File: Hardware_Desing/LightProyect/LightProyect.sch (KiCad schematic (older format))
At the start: 10 parts

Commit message: schematics changes
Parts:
- D1: renamed from D?; footprint (none) -> LightProyect:Neopixel
- J1, J3: renamed from J?; footprint (none) -> TerminalBlock:TerminalBlock_bornier-3_P5.08mm
- J2: renamed from J?; footprint (none) -> TerminalBlock:TerminalBlock_Altech_AK300-3_P5.00mm
- M1: renamed from M?; footprint (none) -> LightProyect:YP8AMS1117_5v_3_3_V
- M2: renamed from M?; footprint (none) -> LightProyect:DC_DC_5V_3V_module
- M3: renamed from M?; footprint (none) -> LightProyect:Audio_Senso_module
- M4: renamed from M?; footprint (none) -> LightProyect:GY-521
- SW1: renamed from SW?; footprint (none) -> Button_Switch_SMD:SW_SPST_TL3305C
- gave numbers to parts that had none: 1
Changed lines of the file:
@@
 $EndDescr
 $Comp
-L power:PWR_FLAG #FLG?
+L power:PWR_FLAG #FLG01
 U 1 1 5EE98E5D
 P 2250 1450
-F 0 "#FLG?" H 2250 1525 50  0001 C CNN
+F 0 "#FLG01" H 2250 1525 50  0001 C CNN
 F 1 "PWR_FLAG" H 2250 1623 50  0000 C CNN
 F 2 "" H 2250 1450 50  0001 C CNN
@@
 $EndComp
 $Comp
-L power:PWR_FLAG #FLG?
+L power:PWR_FLAG #FLG02
 U 1 1 5EE98FDA
 P 3400 3600
-F 0 "#FLG?" H 3400 3675 50  0001 C CNN
+F 0 "#FLG02" H 3400 3675 50  0001 C CNN
 F 1 "PWR_FLAG" H 3350 3750 50  0000 C CNN
 F 2 "" H 3400 3600 50  0001 C CNN
@@
 $EndComp
 $Comp
-L power:VCC #PWR?
+L power:VCC #PWR01
 U 1 1 5EE9959C
 P 1950 1500
-F 0 "#PWR?" H 1950 1350 50  0001 C CNN
+F 0 "#PWR01" H 1950 1350 50  0001 C CNN
 F 1 "VCC" H 1950 1700 50  0000 C CNN
 F 2 "" H 1950 1500 50  0001 C CNN
@@
 $EndComp
 $Comp
-L power:GND #PWR?
+L power:GND #PWR02
 U 1 1 5EE99A46
 P 2700 3600
-F 0 "#PWR?" H 2700 3350 50  0001 C CNN
+F 0 "#PWR02" H 2700 3350 50  0001 C CNN
 F 1 "GND" H 2705 3427 50  0000 C CNN
 F 2 "" H 2700 3600 50  0001 C CNN
@@
 $EndComp
 $Comp
-L RF_Module:ESP-12E U?
+L RF_Module:ESP-12E U1
 U 1 1 5EE9A169
 P 5500 3150
-F 0 "U?" H 5500 4131 50  0000 C CNN
+F 0 "U1" H 5500 4131 50  0000 C CNN
 F 1 "ESP-12E" H 5500 4040 50  0000 C CNN
 F 2 "RF_Module:ESP-12E" H 5500 3150 50  0001 C CNN
@@
 Connection ~ 3400 3600
 $Comp
-L DC_DC_3_5_V_Module:DC_DC_3_5_module M?
+L DC_DC_3_5_V_Module:DC_DC_3_5_module M2
 U 1 1 5EE9F569
 P 3800 1450
-F 0 "M?" H 3912 1815 50  0000 C CNN
+F 0 "M2" H 3912 1815 50  0000 C CNN
 F 1 "DC_DC_3_5_module" H 3912 1724 50  0000 C CNN
-F 2 "" H 3900 1800 50  0001 C CNN
+F 2 "LightProyect:DC_DC_5V_3V_module" H 3900 1800 50  0001 C CNN
 F 3 "" H 3900 1800 50  0001 C CNN
 	1    3800 1450
@@
 $EndComp
 $Comp
-L VoltageRegulator_X_3.3:Regulator_x_3_3 M?
+L VoltageRegulator_X_3.3:Regulator_x_3_3 M1
 U 1 1 5EEA2C27
 P 3700 2350
-F 0 "M?" H 3837 2765 50  0000 C CNN
+F 0 "M1" H 3837 2765 50  0000 C CNN
 F 1 "Regulator_x_3_3" H 3837 2674 50  0000 C CNN
-F 2 "" H 3650 2700 50  0001 C CNN
+F 2 "LightProyect:YP8AMS1117_5v_3_3_V" H 3650 2700 50  0001 C CNN
 F 3 "" H 3650 2700 50  0001 C CNN
 	1    3700 2350
@@
 Connection ~ 4350 3600
 $Comp
-L MPU6050_compressed:MPU6050_lite M?
+L MPU6050_compressed:MPU6050_lite M4
 U 1 1 5EEA9A03
 P 6900 3150
-F 0 "M?" H 7178 3071 50  0000 L CNN
+F 0 "M4" H 7178 3071 50  0000 L CNN
 F 1 "MPU6050_lite" H 7178 2980 50  0000 L CNN
-F 2 "" H 6900 3400 50  0001 C CNN
+F 2 "LightProyect:GY-521" H 6900 3400 50  0001 C CNN
 F 3 "" H 6900 3400 50  0001 C CNN
 	1    6900 3150
@@
 	6300 2750 6100 2750
 $Comp
-L power:GND #PWR?
+L power:GND #PWR06
 U 1 1 5EEB087B
 P 6600 3250
-F 0 "#PWR?" H 6600 3000 50  0001 C CNN
+F 0 "#PWR06" H 6600 3000 50  0001 C CNN
 F 1 "GND" V 6605 3122 50  0000 R CNN
 F 2 "" H 6600 3250 50  0001 C CNN
@@
 $EndComp
 $Comp
-L Connector:AudioJack2_SwitchT J?
+L Connector:AudioJack2_SwitchT J2
 U 1 1 5EEB712D
 P 2000 2250
-F 0 "J?" H 2032 2575 50  0000 C CNN
+F 0 "J2" H 2032 2575 50  0000 C CNN
 F 1 "AudioJack2_SwitchT" H 2032 2484 50  0000 C CNN
-F 2 "" H 2000 2250 50  0001 C CNN
+F 2 "TerminalBlock:TerminalBlock_Altech_AK300-3_P5.00mm" H 2000 2250 50  0001 C CNN
 F 3 "~" H 2000 2250 50  0001 C CNN
 	1    2000 2250
@@
 	7150 2550 7200 2550
 $Comp
-L power:GND #PWR?
+L power:GND #PWR07
 U 1 1 5EEC104A
 P 7200 2550
-F 0 "#PWR?" H 7200 2300 50  0001 C CNN
+F 0 "#PWR07" H 7200 2300 50  0001 C CNN
 F 1 "GND" V 7205 2422 50  0000 R CNN
 F 2 "" H 7200 2550 50  0001 C CNN
@@
 $EndComp
 $Comp
-L Switch:SW_Push SW?
+L Switch:SW_Push SW1
 U 1 1 5EEBFDC3
 P 6950 2550
-F 0 "SW?" H 6950 2835 50  0000 C CNN
+F 0 "SW1" H 6950 2835 50  0000 C CNN
 F 1 "SW_Push" H 6950 2744 50  0000 C CNN
-F 2 "" H 6950 2750 50  0001 C CNN
+F 2 "Button_Switch_SMD:SW_SPST_TL3305C" H 6950 2750 50  0001 C CNN
 F 3 "~" H 6950 2750 50  0001 C CNN
 	1    6950 2550
@@
 $EndComp
 $Comp
-L Connector:Screw_Terminal_01x03 J?
+L Connector:Screw_Terminal_01x03 J3
 U 1 1 5EEC38D8
 P 7400 2800
-F 0 "J?" H 7480 2842 50  0000 L CNN
+F 0 "J3" H 7480 2842 50  0000 L CNN
 F 1 "Screw_Terminal_01x03" H 7480 2751 50  0000 L CNN
-F 2 "" H 7400 2800 50  0001 C CNN
+F 2 "TerminalBlock:TerminalBlock_bornier-3_P5.08mm" H 7400 2800 50  0001 C CNN
 F 3 "~" H 7400 2800 50  0001 C CNN
 	1    7400 2800
@@
 	6750 2900 7200 2900
 $Comp
-L Connector:Screw_Terminal_01x02 J?
+L Connector:Screw_Terminal_01x02 J1
 U 1 1 5EECC20A
 P 1250 2450
-F 0 "J?" H 1168 2125 50  0000 C CNN
+F 0 "J1" H 1168 2125 50  0000 C CNN
 F 1 "Screw_Terminal_01x02" H 1168 2216 50  0000 C CNN
-F 2 "" H 1250 2450 50  0001 C CNN
+F 2 "TerminalBlock:TerminalBlock_bornier-3_P5.08mm" H 1250 2450 50  0001 C CNN
 F 3 "~" H 1250 2450 50  0001 C CNN
 	1    1250 2450
@@
 	1450 3600 2700 3600
 $Comp
-L AudioModule:AudioModule M?
+L AudioModule:AudioModule M3
 U 1 1 5EED2E37
 P 5150 1400
-F 0 "M?" H 5428 1221 50  0000 L CNN
+F 0 "M3" H 5428 1221 50  0000 L CNN
 F 1 "AudioModule" H 5428 1130 50  0000 L CNN
-F 2 "" H 5150 1400 50  0001 C CNN
+F 2 "LightProyect:Audio_Senso_module" H 5150 1400 50  0001 C CNN
 F 3 "" H 5150 1400 50  0001 C CNN
 	1    5150 1400
@@
 	4350 1550 4700 1550
 $Comp
-L power:GND #PWR?
+L power:GND #PWR03
 U 1 1 5EED4411
 P 4850 1750
-F 0 "#PWR?" H 4850 1500 50  0001 C CNN
+F 0 "#PWR03" H 4850 1500 50  0001 C CNN
 F 1 "GND" V 4855 1622 50  0000 R CNN
 F 2 "" H 4850 1750 50  0001 C CNN
@@
 	4750 3350 4900 3350
 $Comp
-L LED:NeoPixel_THT D?
+L LED:NeoPixel_THT D1
 U 1 1 5EED76D3
 P 6150 1400
-F 0 "D?" H 6494 1446 50  0000 L CNN
+F 0 "D1" H 6494 1446 50  0000 L CNN
 F 1 "NeoPixel_THT" H 6494 1355 50  0000 L CNN
-F 2 "" H 6200 1100 50  0001 L TNN
+F 2 "LightProyect:Neopixel" H 6200 1100 50  0001 L TNN
 F 3 "https://www.adafruit.com/product/1938" H 6250 1025 50  0001 L TNN
 	1    6150 1400
@@
 	4700 1550 4850 1550
 $Comp
-L power:GND #PWR?
+L power:GND #PWR04
 U 1 1 5EED96E6
 P 4850 1750
-F 0 "#PWR?" H 4850 1500 50  0001 C CNN
+F 0 "#PWR04" H 4850 1500 50  0001 C CNN
 F 1 "GND" V 4855 1622 50  0000 R CNN
 F 2 "" H 4850 1750 50  0001 C CNN
@@
 Connection ~ 4850 1750
 $Comp
-L power:GND #PWR?
+L power:GND #PWR05
 U 1 1 5EED9B42
 P 6150 1700
-F 0 "#PWR?" H 6150 1450 50  0001 C CNN
+F 0 "#PWR05" H 6150 1450 50  0001 C CNN
 F 1 "GND" H 6155 1527 50  0000 C CNN
 F 2 "" H 6150 1700 50  0001 C CNN

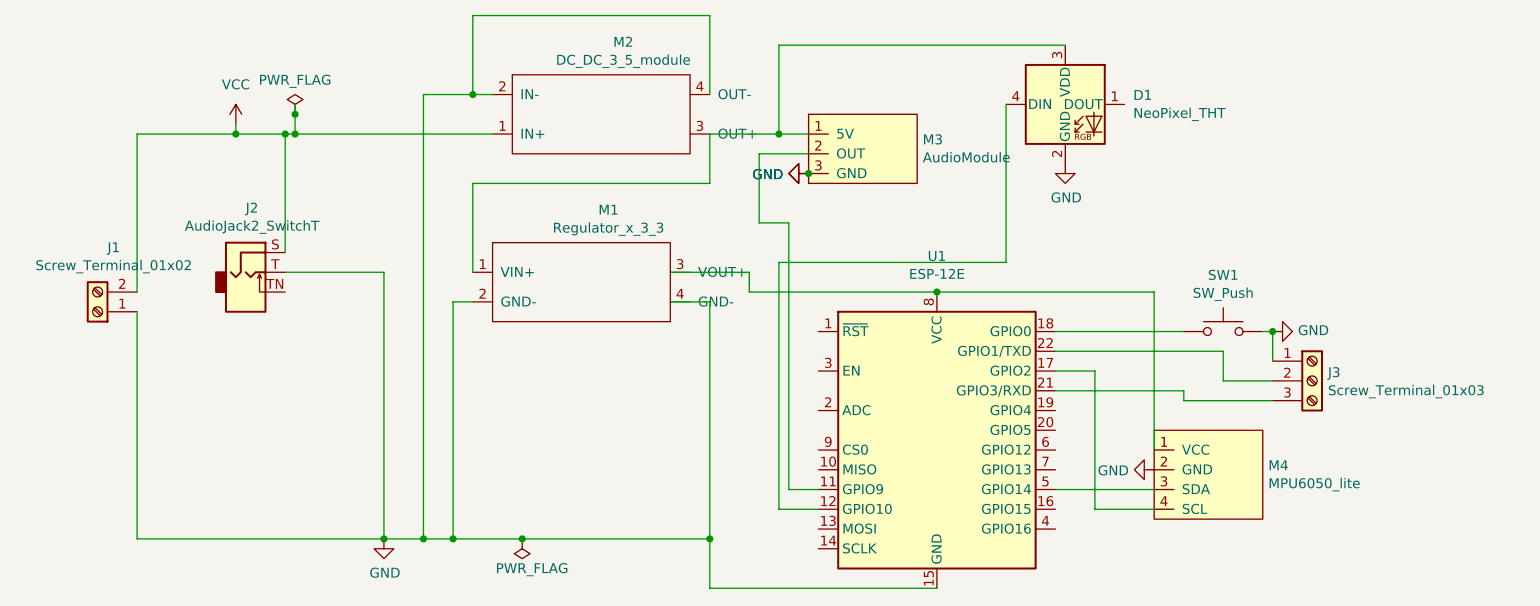
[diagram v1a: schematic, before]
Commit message: PCB and Ifdef pinout
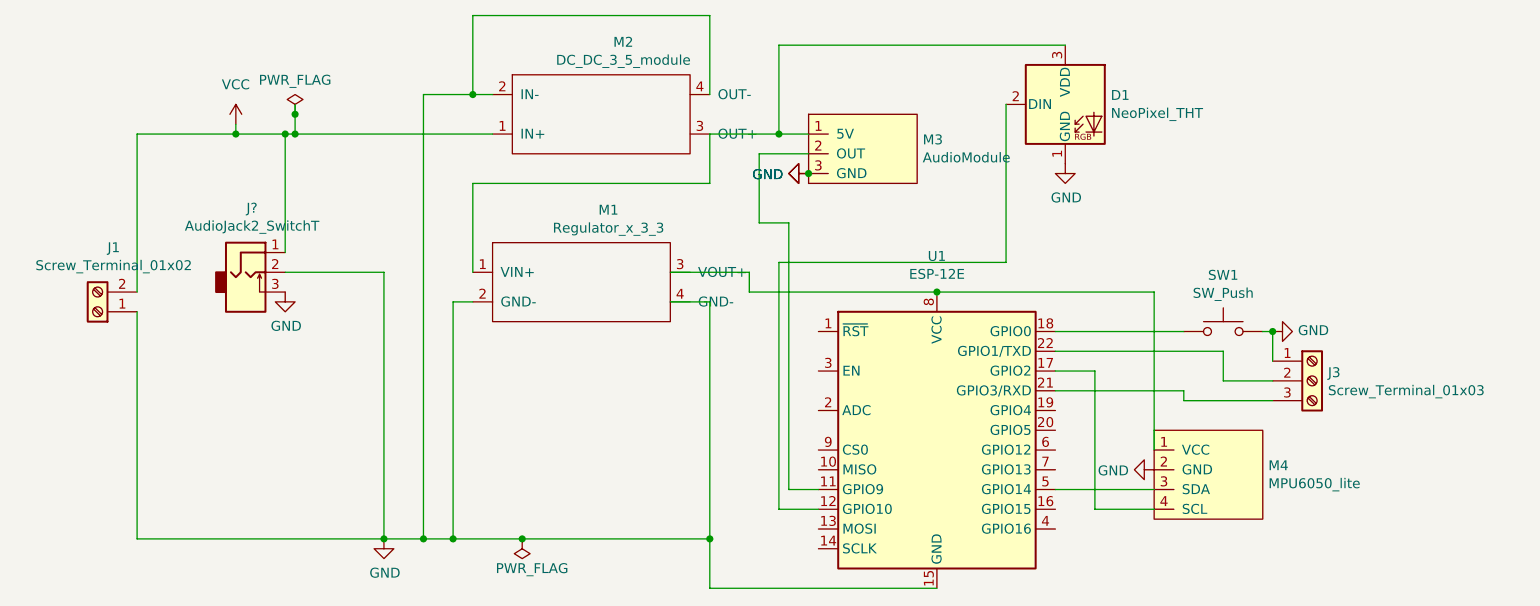
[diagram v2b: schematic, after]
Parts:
- removed D1: NeoPixel_THT, LightProyect:Neopixel, symbol LED:NeoPixel_THT
- removed J2: AudioJack2_SwitchT, TerminalBlock:TerminalBlock_Altech_AK300-3_P5.00mm, symbol Connector:AudioJack2_SwitchT
- added D1: NeoPixel_THT, LightProyect:Neopixel, symbol neopixel_custom:NeoPixel_THT
- added J?: AudioJack2_SwitchT, symbol ONOFF:AudioJack2_SwitchT
- J1: footprint TerminalBlock:TerminalBlock_bornier-3_P5.08mm -> TerminalBlock:TerminalBlock_bornier-2_P5.08mm
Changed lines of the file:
@@
 	0    1    1    0
-$EndComp
-$Comp
-L Connector:AudioJack2_SwitchT J2
-U 1 1 5EEB712D
-P 2000 2250
-F 0 "J2" H 2032 2575 50  0000 C CNN
-F 1 "AudioJack2_SwitchT" H 2032 2484 50  0000 C CNN
-F 2 "TerminalBlock:TerminalBlock_Altech_AK300-3_P5.00mm" H 2000 2250 50  0001 C CNN
-F 3 "~" H 2000 2250 50  0001 C CNN
-	1    2000 2250
-	1    0    0    -1
 $EndComp
 Wire Wire Line
@@
 F 0 "J1" H 1168 2125 50  0000 C CNN
 F 1 "Screw_Terminal_01x02" H 1168 2216 50  0000 C CNN
-F 2 "TerminalBlock:TerminalBlock_bornier-3_P5.08mm" H 1250 2450 50  0001 C CNN
+F 2 "TerminalBlock:TerminalBlock_bornier-2_P5.08mm" H 1250 2450 50  0001 C CNN
 F 3 "~" H 1250 2450 50  0001 C CNN
 	1    1250 2450
@@
 Wire Wire Line
 	4750 3350 4900 3350
-$Comp
-L LED:NeoPixel_THT D1
-U 1 1 5EED76D3
-P 6150 1400
-F 0 "D1" H 6494 1446 50  0000 L CNN
-F 1 "NeoPixel_THT" H 6494 1355 50  0000 L CNN
-F 2 "LightProyect:Neopixel" H 6200 1100 50  0001 L TNN
-F 3 "https://www.adafruit.com/product/1938" H 6250 1025 50  0001 L TNN
-	1    6150 1400
-	1    0    0    -1
-$EndComp
 Wire Wire Line
 	6150 1100 4700 1100
@@
 Wire Wire Line
 	4700 3450 4900 3450
+$Comp
+L power:GND #PWR08
+U 1 1 5EF010D0
+P 2200 2350
+F 0 "#PWR08" H 2200 2100 50  0001 C CNN
+F 1 "GND" H 2205 2177 50  0000 C CNN
+F 2 "" H 2200 2350 50  0001 C CNN
+F 3 "" H 2200 2350 50  0001 C CNN
+	1    2200 2350
+	1    0    0    -1
+$EndComp
+$Comp
+L neopixel_custom:NeoPixel_THT D1
+U 1 1 5EF06E3B
+P 6150 1400
+F 0 "D1" H 6380 1446 50  0000 L CNN
+F 1 "NeoPixel_THT" H 6380 1355 50  0000 L CNN
+F 2 "LightProyect:Neopixel" H 6200 1100 50  0001 L TNN
+F 3 "https://www.adafruit.com/product/1938" H 6250 1025 50  0001 L TNN
+	1    6150 1400
+	1    0    0    -1
+$EndComp
+$Comp
+L ONOFF:AudioJack2_SwitchT J?
+U 1 1 5EF4A436
+P 2000 2250
+F 0 "J?" H 2032 2575 50  0000 C CNN
+F 1 "AudioJack2_SwitchT" H 2032 2484 50  0000 C CNN
+F 2 "" H 2000 2250 50  0001 C CNN
+F 3 "~" H 2000 2250 50  0001 C CNN
+	1    2000 2250
+	1    0    0    -1
+$EndComp
 $EndSCHEMATC

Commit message: linux fix
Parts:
- D1: symbol neopixel_custom:NeoPixel_THT -> LightProyect-rescue:NeoPixel_THT-neopixel_custom
- J2: renamed from J?; footprint (none) -> TerminalBlock:TerminalBlock_bornier-3_P5.08mm; symbol ONOFF:AudioJack2_SwitchT -> LightProyect-rescue:AudioJack2_SwitchT-ONOFF
- M1: symbol VoltageRegulator_X_3.3:Regulator_x_3_3 -> LightProyect-rescue:Regulator_x_3_3-VoltageRegulator_X_3.3
- M2: symbol DC_DC_3_5_V_Module:DC_DC_3_5_module -> LightProyect-rescue:DC_DC_3_5_module-DC_DC_3_5_V_Module
- M3: symbol AudioModule:AudioModule -> LightProyect-rescue:AudioModule-AudioModule
- M4: symbol MPU6050_compressed:MPU6050_lite -> LightProyect-rescue:MPU6050_lite-MPU6050_compressed
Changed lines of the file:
@@
 Connection ~ 3400 3600
 $Comp
-L DC_DC_3_5_V_Module:DC_DC_3_5_module M2
+L LightProyect-rescue:DC_DC_3_5_module-DC_DC_3_5_V_Module M2
 U 1 1 5EE9F569
 P 3800 1450
@@
 $EndComp
 $Comp
-L VoltageRegulator_X_3.3:Regulator_x_3_3 M1
+L LightProyect-rescue:Regulator_x_3_3-VoltageRegulator_X_3.3 M1
 U 1 1 5EEA2C27
 P 3700 2350
@@
 Connection ~ 4350 3600
 $Comp
-L MPU6050_compressed:MPU6050_lite M4
+L LightProyect-rescue:MPU6050_lite-MPU6050_compressed M4
 U 1 1 5EEA9A03
 P 6900 3150
@@
 	1450 3600 2700 3600
 $Comp
-L AudioModule:AudioModule M3
+L LightProyect-rescue:AudioModule-AudioModule M3
 U 1 1 5EED2E37
 P 5150 1400
@@
 $EndComp
 $Comp
-L neopixel_custom:NeoPixel_THT D1
+L LightProyect-rescue:NeoPixel_THT-neopixel_custom D1
 U 1 1 5EF06E3B
 P 6150 1400
@@
 $EndComp
 $Comp
-L ONOFF:AudioJack2_SwitchT J?
+L LightProyect-rescue:AudioJack2_SwitchT-ONOFF J2
 U 1 1 5EF4A436
 P 2000 2250
-F 0 "J?" H 2032 2575 50  0000 C CNN
+F 0 "J2" H 2032 2575 50  0000 C CNN
 F 1 "AudioJack2_SwitchT" H 2032 2484 50  0000 C CNN
-F 2 "" H 2000 2250 50  0001 C CNN
+F 2 "TerminalBlock:TerminalBlock_bornier-3_P5.08mm" H 2000 2250 50  0001 C CNN
 F 3 "~" H 2000 2250 50  0001 C CNN
 	1    2000 2250
